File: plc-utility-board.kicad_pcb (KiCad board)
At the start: 2 copper layers, 117 parts, among them J1 Screw_Terminal_01x02, J10 Screw_Terminal_01x03, J11 Screw_Terminal_01x02, J2 Screw_Terminal_01x08, J3 Screw_Terminal_01x04, J4 Screw_Terminal_01x08, J5 Screw_Terminal_01x04, J6 Conn_01x03_Male, J7 Conn_01x03_Male, J8 Screw_Terminal_01x03, J9 Screw_Terminal_01x02, Q1 2N7002, Q10 2N7002, Q11 2N7002, Q12 2N7002, Q13 FDV304, Q14 2N7002, Q15 2N7002, Q16 2N7002, Q2 2N7002, Q3 Q_PMOS_GSD, Q4 Q_PMOS_GSD, Q5 2N7002, Q6 2N7002, Q7 Q_PMOS_GSD, Q8 Q_PMOS_GSD, Q9 FDV304, SW1 SW_Push, SW2 SW_Push, SW3 SW_Push, SW4 SW_Push, SW5 SW_Push, SW6 SW_Push, U1 L78L33_SOT89, U2 DRV8840, U3 DRV8840

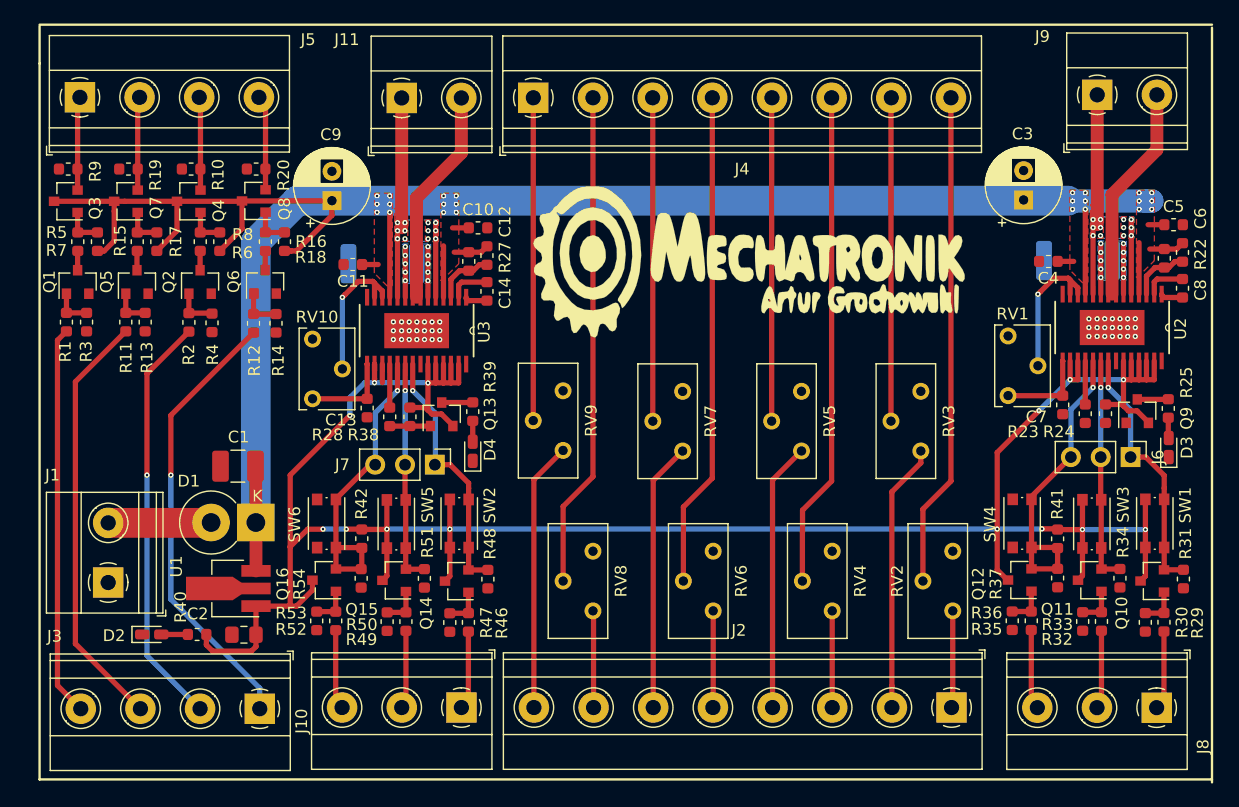
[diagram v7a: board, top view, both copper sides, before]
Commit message: Added HTSSOP 28 3d model for motor controller
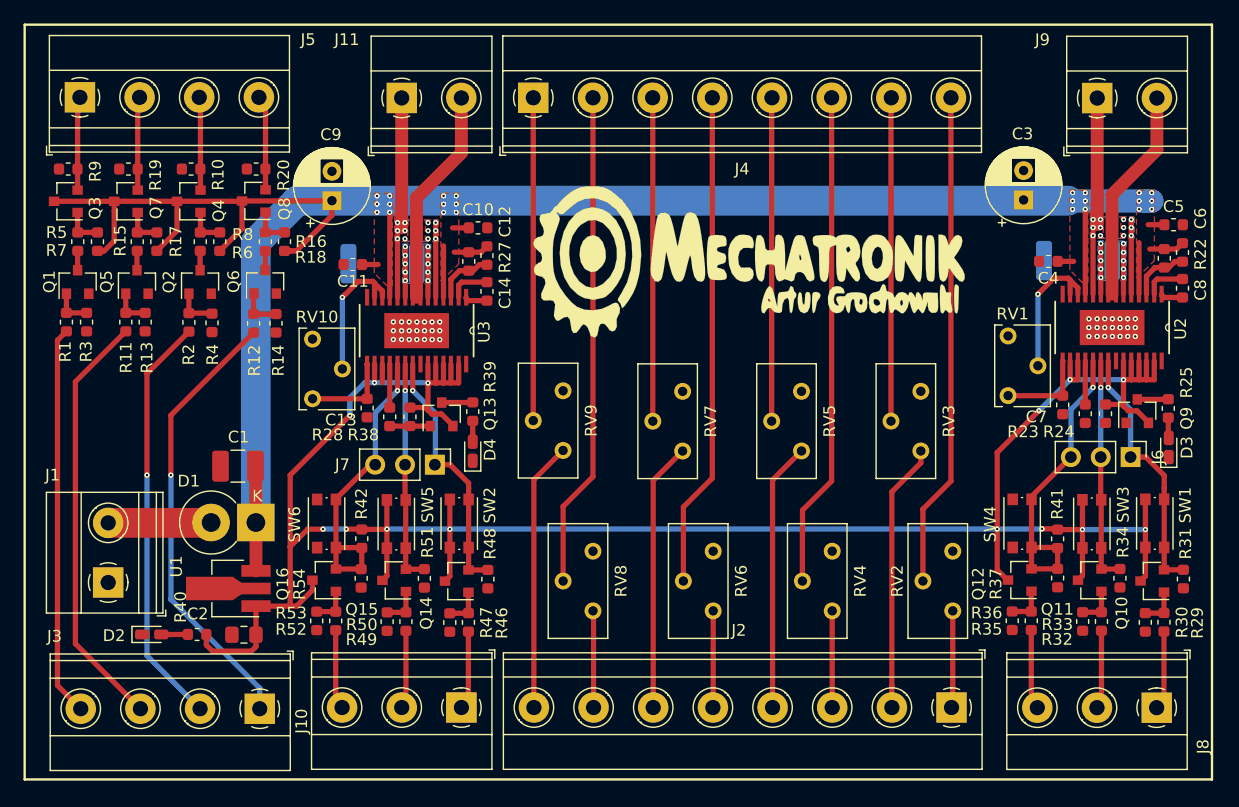
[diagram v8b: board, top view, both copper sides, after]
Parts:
- moved J9 0.28 mm to (191.7, 69.0)
